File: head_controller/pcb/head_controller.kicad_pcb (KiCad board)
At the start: 2 copper layers, 85.6 x 132.3 mm, 79 parts, among them P1 HEADER_02X08_SMD, P2 HEADER_02X05_SMD, U1 HALL_DRV5053, U10 MAX4215, U11 HALL_DRV5053, U12 MAX4215, U13 HALL_DRV5053, U14 MAX4215, U2 MAX4215, U3 HALL_DRV5053, U4 MAX4215, U5 HALL_DRV5053, U6 MAX4215, U7 HALL_DRV5053, U8 MAX4215, U9 HALL_DRV5053

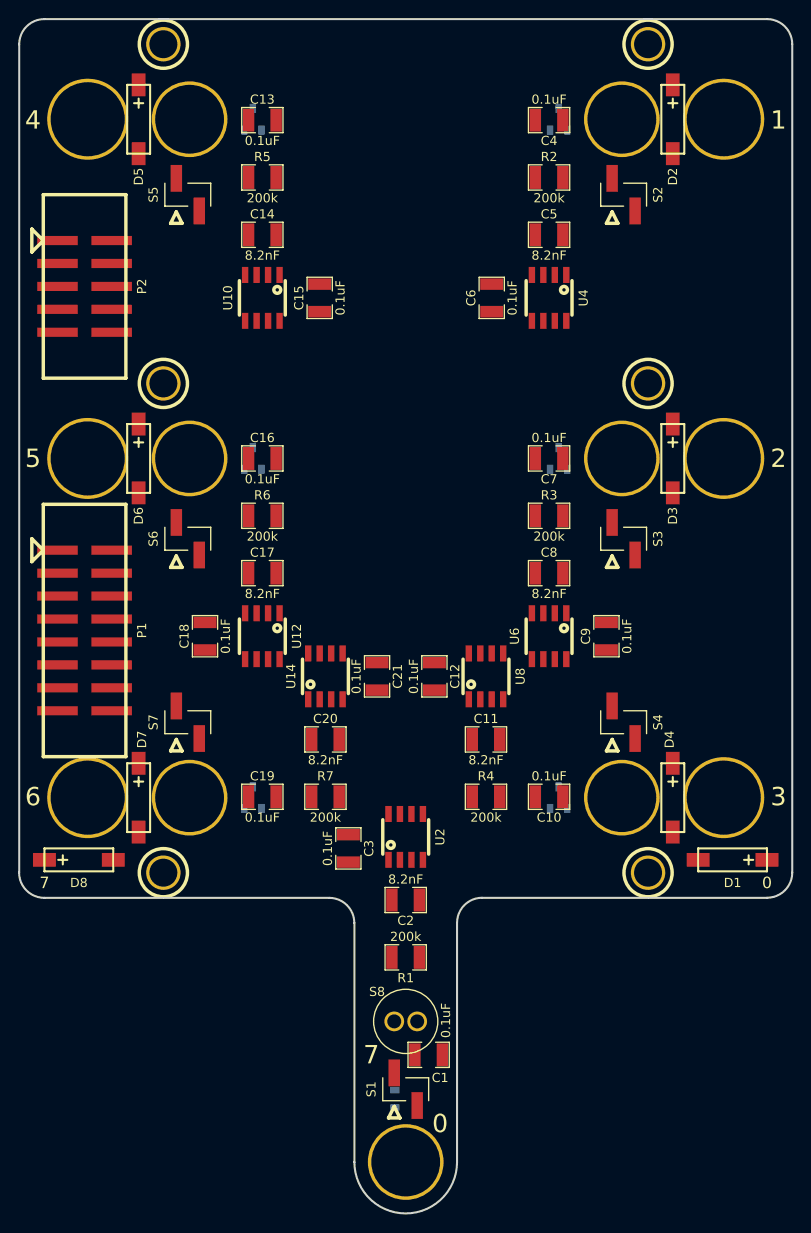
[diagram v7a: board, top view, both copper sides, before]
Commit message: Moved edge cut graphics to create dsn file.
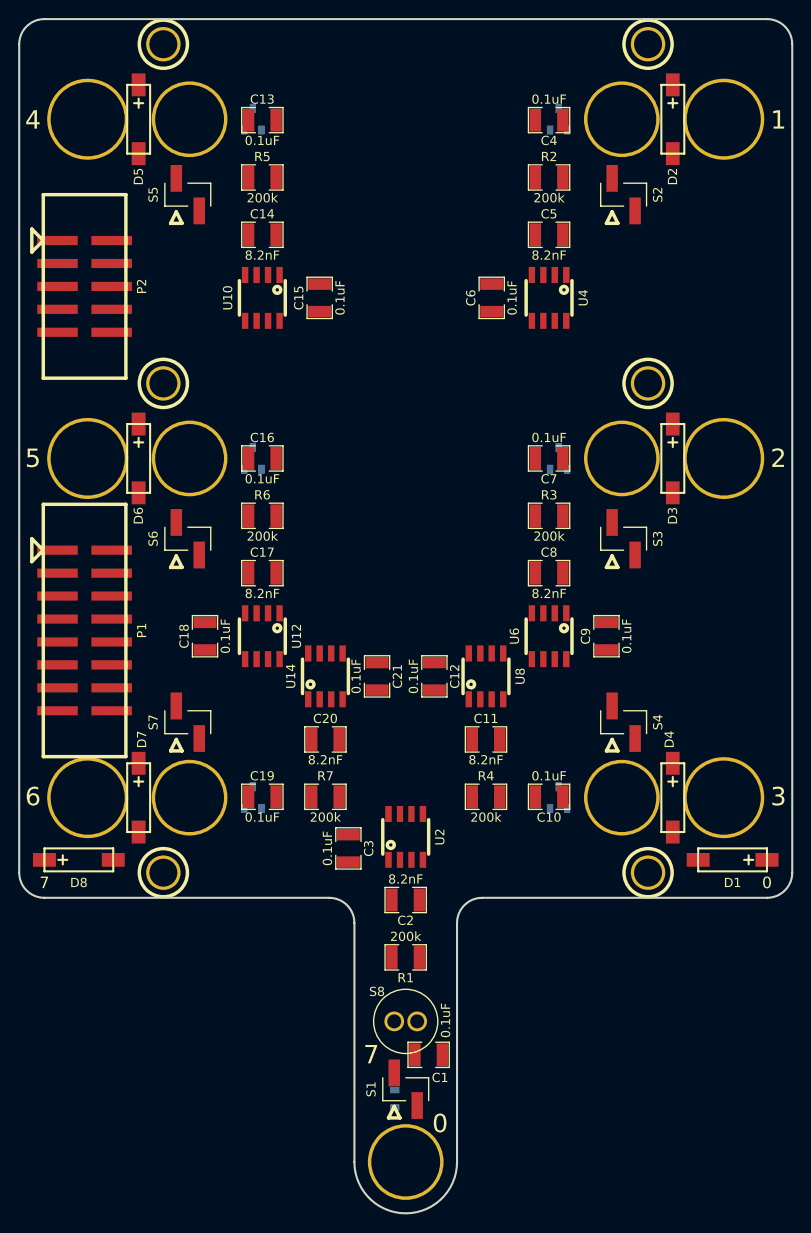
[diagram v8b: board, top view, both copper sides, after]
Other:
- board size 85.6 x 132.3 mm -> 85.6 x 132.2 mm
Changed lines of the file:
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@@
     (effects (font (size 2.032 2.032) (thickness 0.508)))
   )
-  (gr_arc (start 93.599 151.9682) (end 99.28352 151.9682) (angle 180) (layer Edge.Cuts) (width 0.2286))
-  (gr_line (start 99.28352 125.476) (end 99.28352 151.9682) (angle 90) (layer Edge.Cuts) (width 0.2286))
-  (gr_line (start 87.91702 125.476) (end 87.91702 151.9682) (angle 90) (layer Edge.Cuts) (width 0.2286))
-  (gr_arc (start 102.06482 125.476) (end 99.28352 125.476) (angle 90) (layer Edge.Cuts) (width 0.2286))
-  (gr_arc (start 85.13572 125.476) (end 85.13572 122.7074) (angle 90) (layer Edge.Cuts) (width 0.2286))
-  (gr_line (start 102.06482 122.7074) (end 133.61924 122.7074) (angle 90) (layer Edge.Cuts) (width 0.2286))
-  (gr_line (start 53.5813 122.7074) (end 85.13572 122.7074) (angle 90) (layer Edge.Cuts) (width 0.2286))
+  (gr_arc (start 93.599 151.95804) (end 99.28352 151.95804) (angle 180) (layer Edge.Cuts) (width 0.2286))
+  (gr_line (start 99.28352 125.48362) (end 99.28352 151.95804) (angle 90) (layer Edge.Cuts) (width 0.2286))
+  (gr_line (start 87.91702 125.48362) (end 87.91702 151.95804) (angle 90) (layer Edge.Cuts) (width 0.2286))
+  (gr_arc (start 102.06482 125.48362) (end 99.28352 125.48362) (angle 90) (layer Edge.Cuts) (width 0.2286))
+  (gr_arc (start 85.13572 125.48362) (end 85.13572 122.70232) (angle 90) (layer Edge.Cuts) (width 0.2286))
+  (gr_line (start 102.06482 122.70232) (end 133.61924 122.70232) (angle 90) (layer Edge.Cuts) (width 0.2286))
+  (gr_line (start 53.5813 122.70232) (end 85.13572 122.70232) (angle 90) (layer Edge.Cuts) (width 0.2286))
   (gr_arc (start 53.5813 28.1813) (end 50.8 28.1813) (angle 90) (layer Edge.Cuts) (width 0.2286))
-  (gr_arc (start 133.61924 119.9134) (end 136.40054 119.9134) (angle 90) (layer Edge.Cuts) (width 0.2286))
-  (gr_line (start 136.40054 28.194) (end 136.40054 119.9134) (angle 90) (layer Edge.Cuts) (width 0.2286))
-  (gr_arc (start 53.5813 119.9134) (end 53.5813 122.7074) (angle 90) (layer Edge.Cuts) (width 0.2286))
-  (gr_line (start 50.8 28.194) (end 50.8 119.9134) (angle 90) (layer Edge.Cuts) (width 0.2286))
+  (gr_arc (start 133.61924 119.92102) (end 136.40054 119.92102) (angle 90) (layer Edge.Cuts) (width 0.2286))
+  (gr_line (start 136.40054 28.1813) (end 136.40054 119.92102) (angle 90) (layer Edge.Cuts) (width 0.2286))
+  (gr_arc (start 53.5813 119.92102) (end 53.5813 122.70232) (angle 90) (layer Edge.Cuts) (width 0.2286))
+  (gr_line (start 50.8 28.1813) (end 50.8 119.92102) (angle 90) (layer Edge.Cuts) (width 0.2286))
   (gr_arc (start 133.61924 28.1813) (end 133.61924 25.4) (angle 90) (layer Edge.Cuts) (width 0.2286))
   (gr_line (start 53.5813 25.4) (end 133.61924 25.4) (angle 90) (layer Edge.Cuts) (width 0.2286))
